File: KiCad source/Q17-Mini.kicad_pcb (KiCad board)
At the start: 2 copper layers, 95 x 75 mm, 85 parts, among them J1 Input, J2-1 SPK+, J2-2 SPK-, J3-1 V+, J3-2 GND, J3-3 V-, Q1 IRF610, Q10 KSA992, Q11 BS250P, Q12 BD139, Q13 IRF610, Q14 IRF9610, Q15 FQA46N15, Q16 FQA36P15, Q2 KSA992, Q3 KSC1845, Q4 IRF9610, Q5 FQP3P20, Q6 FQP3N30, Q7 KSC1845, Q8 ZVN4206AV, Q9 BS250P, U1 OPA1641, U1' OPA1641

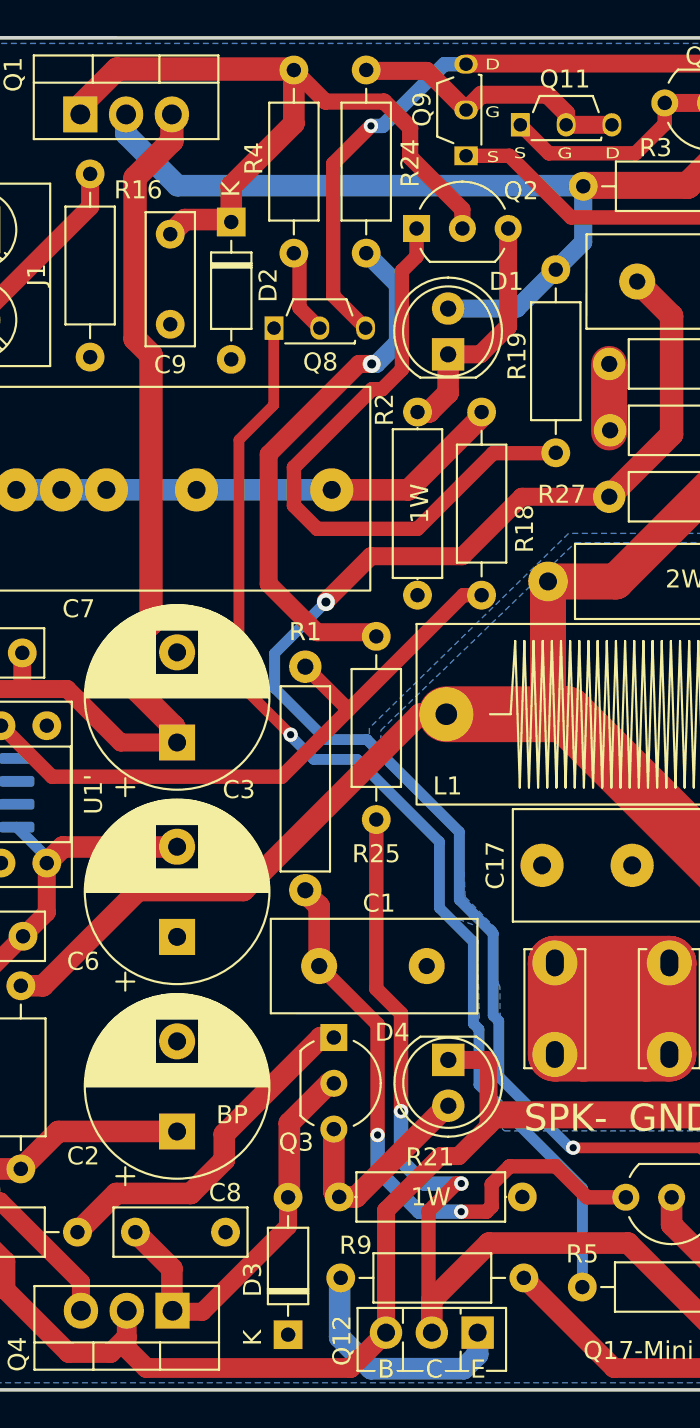
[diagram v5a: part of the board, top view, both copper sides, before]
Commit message: PCB v1.0.9
- Moved Q8 and deleted a track on back PCB.
- Some comments added on schematic.
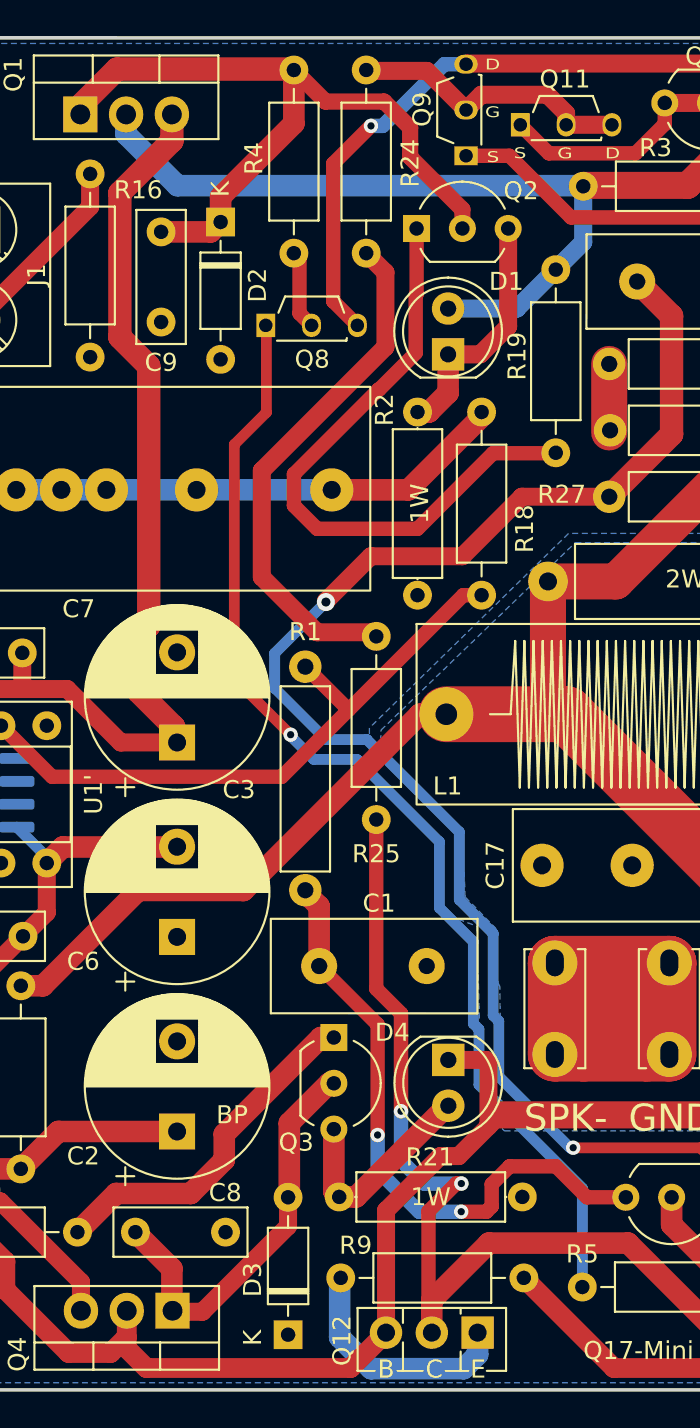
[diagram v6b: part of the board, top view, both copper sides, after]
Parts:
- moved D2 0.59 mm to (119.6, 65.3)
- moved C9 0.52 mm to (116.3, 70.8)
- moved Q8 0.48 mm to (122.1, 71.0)
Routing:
- net Net-(R24-Pad2): track 29.8 -> 29.0 mm, vias 1 -> 0
- net Net-(C3-Pad1): track 57.7 -> 58.3 mm

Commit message: PCB v1.0.1 PRODUCTION
First production version.
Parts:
- moved Q12 5.17 mm to (128.8, 127.6), turned to 0 degrees
- moved D3 1.27 mm to (123.4, 125.7)
- moved R9 0.67 mm to (126.2, 123.2)
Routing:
- net Net-(C12-Pad2): track 144.1 -> 166.4 mm
- net Net-(Q12-Pad1): track 13.2 -> 5.49 mm
- net Net-(Q12-Pad2): track 58.9 -> 60.8 mm
- net Net-(Q6-Pad3): track 72.3 -> 73.0 mm
- net Net-(C14-Pad2): track 45.3 -> 45.9 mm
- net Net-(C10-Pad2): vias 2 -> 1
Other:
- board text added: "Q17-Mini 1.1.0"
- board text added: "QUAD405 Audiophile Circuit design by Tiberiu Vicol PCB design by Stef PROTO RELEASE 2022"
- board text added: "Use a Speaker Protection Board."
- board text removed: "Q17-Mini 1.0.9"
- board text removed: "QUAD405 Audiophile Circuit design by Tiberiu Vicol PCB design by Stef PROTO RELEASE 2021"
- board text removed: "Use a Speaker Protection Board or add 1uF MKP capacitor at input."
